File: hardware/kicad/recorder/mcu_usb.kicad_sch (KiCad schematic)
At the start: 13 parts, among them J1 UART0, J2 USB_C_16P, U1 ESP32-S3-MINI-1U-N8, U7 USBLC6-2SC6

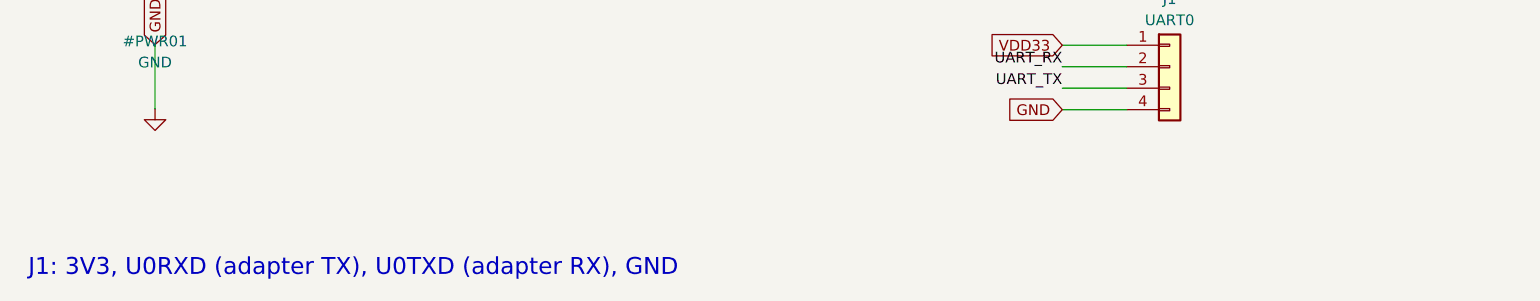
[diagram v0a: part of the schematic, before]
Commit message: Keep J1 off SMT and fix MK1 pinout plus the 2.8 V analog rail.
J1 is a vertical 1x4 that will not fit under the lid, and the tails poke
toward the phone. Flag it exclude_from_bom so JLCPCB does not wave-solder
it. Keep C124378 in docs/bom.md and write jlcpcb_extra.csv so the header
can still be ordered as loose extra parts.

IM73A135 pin 3 is OUT-, a ~250 ohm amplifier output, not GND. Leave it
open; C15 still AC-couples OUT+ and C16 still takes codec MIC_N to AGND.
U8 is now LP5907-2.8 (C186700) because the capsule VDD abs max is 3.0 V.
ES8311 AVDD is 1.7-3.6 V and Y1 is 1.71-3.63 V, so the analog island can
sit at 2.8 V. Digital IO stays on VDD33.

Co-authored-by: zachrobertson19 <zachrobertson19@gmail.com>
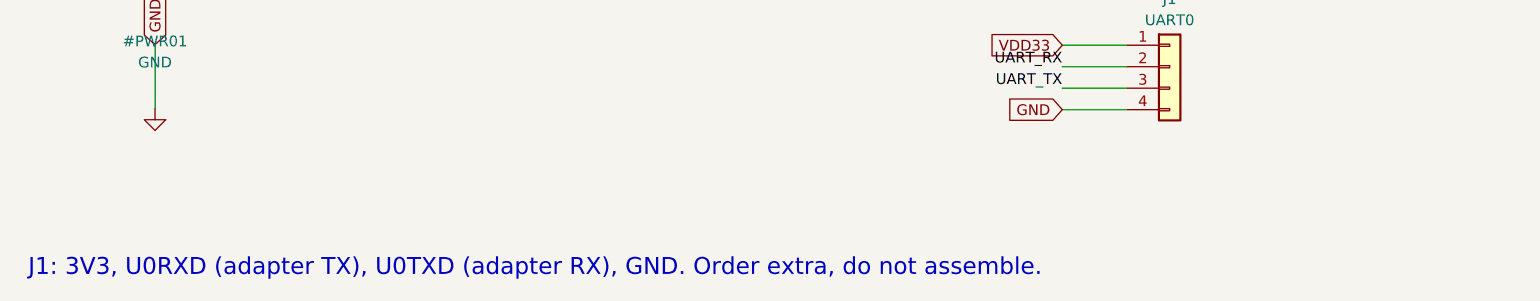
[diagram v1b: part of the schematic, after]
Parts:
- J1: now left out of the parts list
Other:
- note added: "J1: 3V3, U0RXD (adapter TX), U0TXD (adapter RX), GND. Order extra, do not assemble."
- note removed: "J1: 3V3, U0RXD (adapter TX), U0TXD (adapter RX), GND"
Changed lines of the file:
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@@
 		(unit 1)
 		(exclude_from_sim no)
-		(in_bom yes)
+		(in_bom no)
 		(on_board yes)
 		(dnp no)
@@
 		(effects (font (size 1.27 1.27)) (justify right))
 	)
-	(text "J1: 3V3, U0RXD (adapter TX), U0TXD (adapter RX), GND"
+	(text "J1: 3V3, U0RXD (adapter TX), U0TXD (adapter RX), GND. Order extra, do not assemble."
 		(exclude_from_sim no)
 		(at 25.00 200.00 0)
